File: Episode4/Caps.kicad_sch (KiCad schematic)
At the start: 190 parts

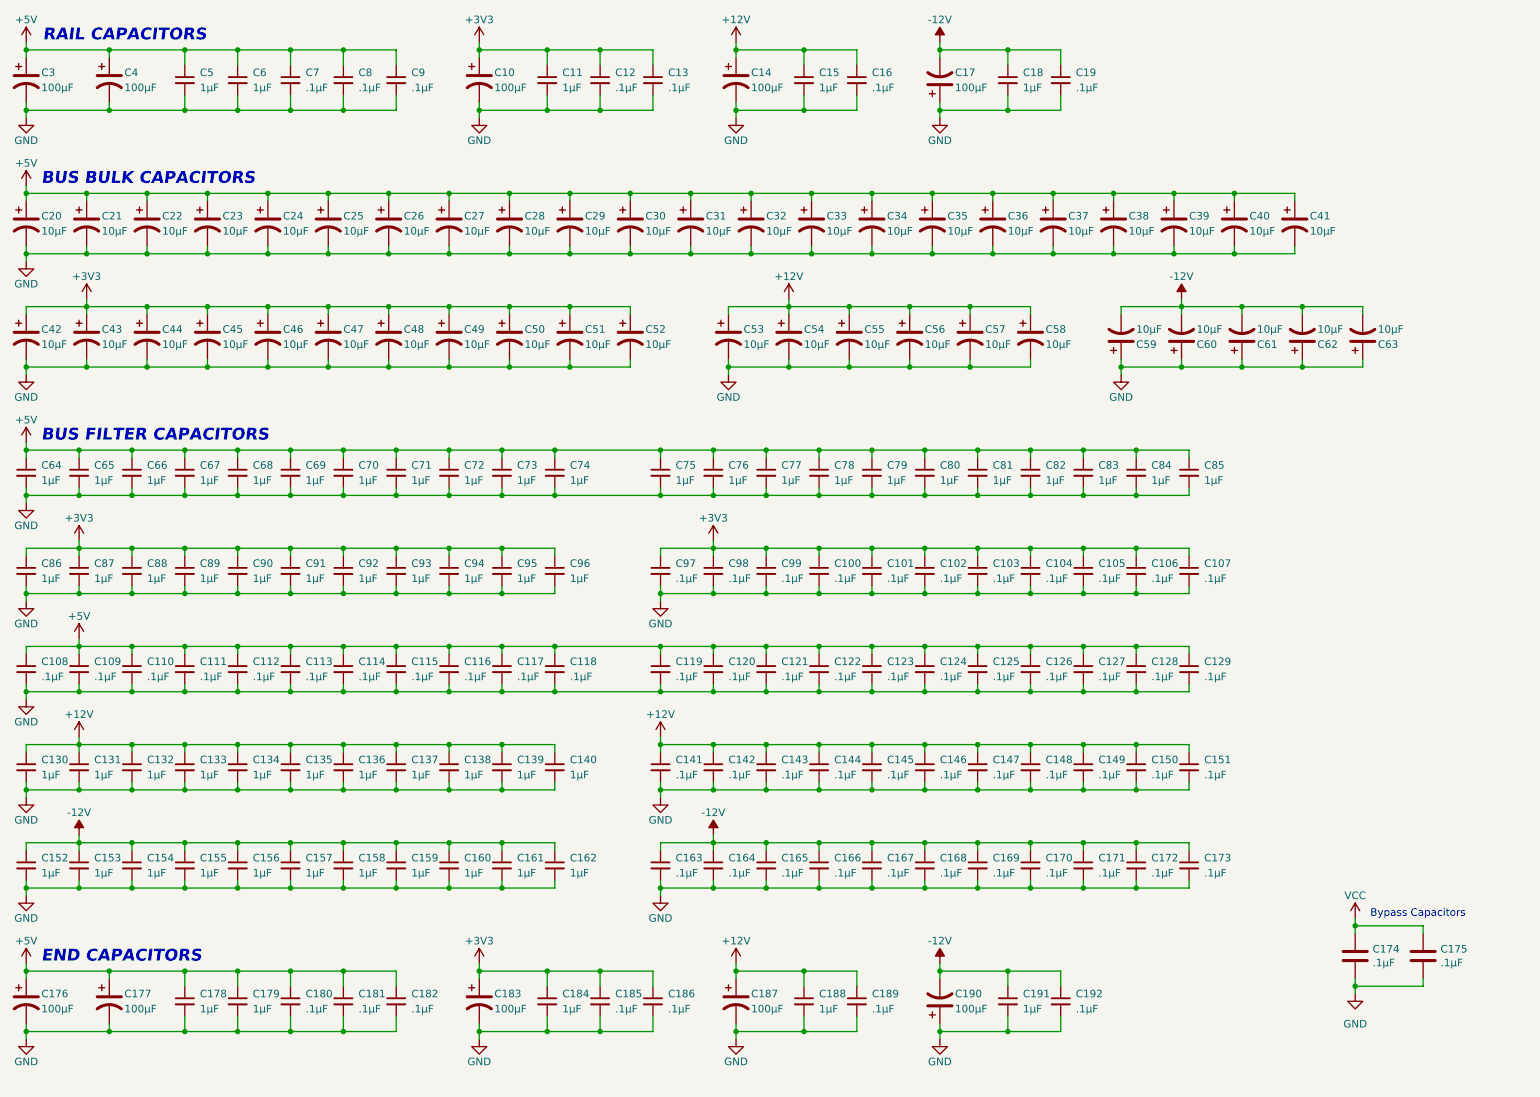
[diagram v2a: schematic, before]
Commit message: Reworked bus line order, capacitor and trace placement
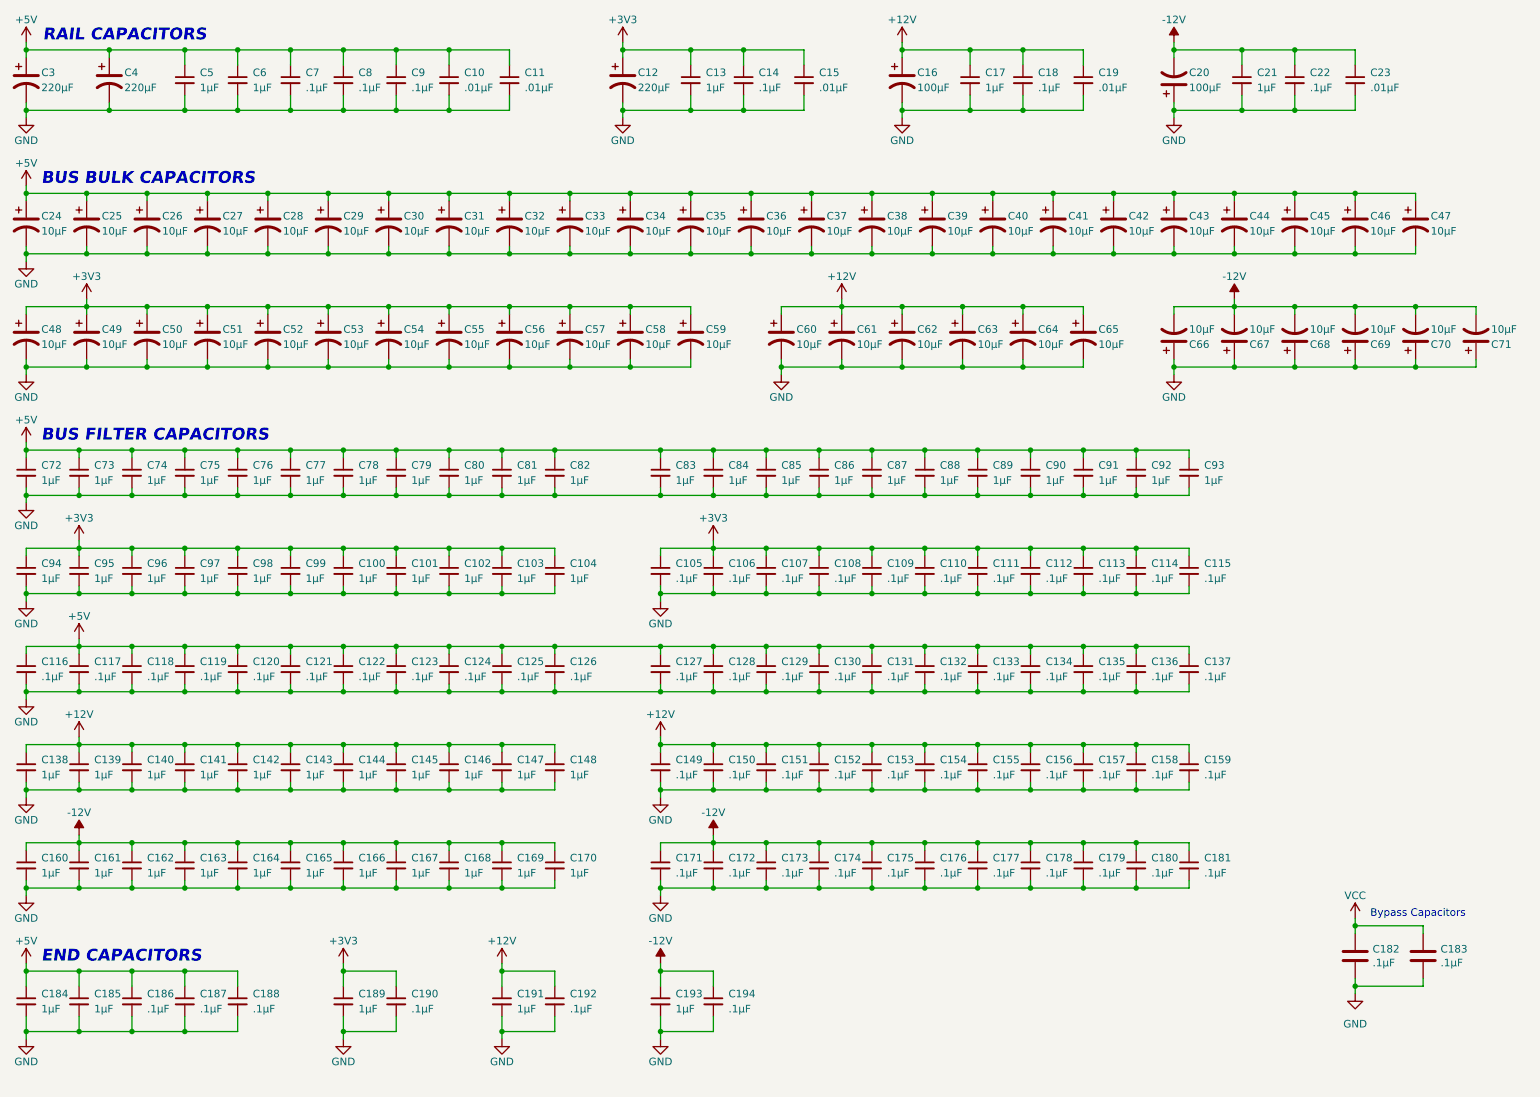
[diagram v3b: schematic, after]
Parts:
- removed C13, C186: .1µF, Capacitor_SMD:C_0805_2012Metric_Pad1.18x1.45mm_HandSolder, symbol Device:C_Small
- removed C176, C177, C183, C187, C190: 100µF, Capacitor_SMD:CP_Elec_6.3x7.7, symbol Device:C_Polarized_US
- added C10, C11, C15, C19, C23: .01µF, Capacitor_SMD:C_0805_2012Metric_Pad1.18x1.45mm_HandSolder, symbol Device:C_Small
- added C46, C47, C59, C71: 10µF, Capacitor_SMD:CP_Elec_4x5.8, symbol Device:C_Polarized_US
- C12: renamed from C10; value 100µF -> 220µF; Manufacturer_Part_Number UCD1E101MCL1GS -> UCD1C221MCL1GS
- C3, C4: value 100µF -> 220µF; Manufacturer_Part_Number UCD1E101MCL1GS -> UCD1C221MCL1GS
- renumbered C92 to C100, C93 to C101, C94 to C102, C95 to C103, C96 to C104, C97 to C105, C98 to C106, C99 to C107, C100 to C108, C101 to C109, C102 to C110, C103 to C111, C104 to C112, C105 to C113, C106 to C114, C107 to C115, C108 to C116, C109 to C117, C110 to C118, C111 to C119, C112 to C120, C113 to C121, C114 to C122, C115 to C123, C116 to C124, C117 to C125, C118 to C126, C119 to C127, C120 to C128, C121 to C129, C11 to C13, C122 to C130, C123 to C131, C124 to C132, C125 to C133, C126 to C134, C127 to C135, C128 to C136, C129 to C137, C130 to C138, C131 to C139, C12 to C14, C132 to C140, C133 to C141, C134 to C142, C135 to C143, C136 to C144, C137 to C145, C138 to C146, C139 to C147, C140 to C148, C141 to C149, C142 to C150, C143 to C151, C144 to C152, C145 to C153, C146 to C154, C147 to C155, C148 to C156, C149 to C157, C150 to C158, C151 to C159, C14 to C16, C152 to C160, C153 to C161, C154 to C162, C155 to C163, C156 to C164, C157 to C165, C158 to C166, C159 to C167, C160 to C168, C161 to C169, C15 to C17, C162 to C170, C163 to C171, C164 to C172, C165 to C173, C166 to C174, C167 to C175, C168 to C176, C169 to C177, C170 to C178, C171 to C179, C16 to C18, C172 to C180, C173 to C181, C174 to C182, C175 to C183, C178 to C184, C179 to C185, C180 to C186, C181 to C187, C182 to C188, C184 to C189, C185 to C190, C188 to C191, C189 to C192, C191 to C193, C192 to C194, C17 to C20, C18 to C21, C19 to C22, C20 to C24, C21 to C25, C22 to C26, C23 to C27, C24 to C28, C25 to C29, C26 to C30, C27 to C31, C28 to C32, C29 to C33, C30 to C34, C31 to C35, C32 to C36, C33 to C37, C34 to C38, C35 to C39, C36 to C40, C37 to C41, C38 to C42, C39 to C43, C40 to C44, C41 to C45, C42 to C48, C43 to C49, C44 to C50, C45 to C51, C46 to C52, C47 to C53, C48 to C54, C49 to C55, C50 to C56, C51 to C57, C52 to C58, C53 to C60, C54 to C61, C55 to C62, C56 to C63, C57 to C64, C58 to C65, C59 to C66, C60 to C67, C61 to C68, C62 to C69, C63 to C70, C64 to C72, C65 to C73, C66 to C74, C67 to C75, C68 to C76, C69 to C77, C70 to C78, C71 to C79, C72 to C80, C73 to C81, C74 to C82, C75 to C83, C76 to C84, C77 to C85, C78 to C86, C79 to C87, C80 to C88, C81 to C89, C82 to C90, C83 to C91, C84 to C92, C85 to C93, C86 to C94, C87 to C95, C88 to C96, C89 to C97, C90 to C98, C91 to C99
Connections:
- net +12V: now also C19.1
- net +3V3: now also C15.1, C59.1
- net +5V: now also C10.1, C11.1, C46.1, C47.1
- net -12V: now also C23.1, C71.2
- net GND: now also C10.2, C11.2, C15.2, C19.2, C23.2, C46.2, C47.2, C59.2, C71.1
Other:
- moved on the sheet: C12, C13, C14, C16, C17, C18, C184, C185, C186, C187, C188, C189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

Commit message: Finished the backplane
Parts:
- removed C144, C145, C146, C147, C148, C165, C166, C167, C168, C169, C170, C191, C193: 1µF, Capacitor_SMD:C_0805_2012Metric_Pad1.18x1.45mm_HandSolder, symbol Device:C_Small
- removed C155, C156, C159, C171, C172, C173, C174, C175, C176, C188, C192, C194, C8: .1µF, Capacitor_SMD:C_0805_2012Metric_Pad1.18x1.45mm_HandSolder, symbol Device:C_Small
- removed C182, C183: .1µF, Capacitor_SMD:C_0805_2012Metric_Pad1.18x1.45mm_HandSolder, symbol Device:C
- added C118, C129, C148, C159, C179, C28, C39, C58, C69, C8, C88, C99: 10µF, Capacitor_SMD:CP_Elec_4x5.8, symbol Device:C_Polarized_Small_US
- added C119, C128, C149, C180, C29, C38, C59, C68, C7, C89, C98: 1µF, Capacitor_SMD:C_0805_2012Metric_Pad1.18x1.45mm_HandSolder, symbol Device:C_Small
- added C120, C127, C150, C181, C30, C37, C6, C60, C67, C90, C97: 0.1µF, Capacitor_SMD:C_0805_2012Metric_Pad1.18x1.45mm_HandSolder, symbol Device:C_Small
- added C14, C15, C4, C5, C9: 10nF, Capacitor_SMD:C_0805_2012Metric_Pad1.18x1.45mm_HandSolder, symbol Device:C_Small
- C1: renamed from C46; symbol Device:C_Polarized_US -> Device:C_Polarized_Small_US
- C10: renamed from C187; value .1µF -> 0.1µF; Manufacturer_Name Samsung Electro-Mechanics -> TAIYO YUDEN; Manufacturer_Part_Number CL21B104KBFNNNG -> MCASU21GSB7104KTNA01
- C100: renamed from C110; value .1µF -> 0.1µF; Manufacturer_Name Samsung Electro-Mechanics -> TAIYO YUDEN; Manufacturer_Part_Number CL21B104KBFNNNG -> MCASU21GSB7104KTNA01
- C101: renamed from C99; Manufacturer_Name Samsung Electro-Mechanics -> TAIYO YUDEN; Manufacturer_Part_Number CL21B105KBFNNNG -> MCASU21GSB7105KTNA01
- C102: renamed from C48; symbol Device:C_Polarized_US -> Device:C_Polarized_Small_US
- C103: renamed from C67; symbol Device:C_Polarized_US -> Device:C_Polarized_Small_US
- C104: renamed from C162; Manufacturer_Name Samsung Electro-Mechanics -> TAIYO YUDEN; Manufacturer_Part_Number CL21B105KBFNNNG -> MCASU21GSB7105KTNA01
- C105: renamed from C179; value .1µF -> 0.1µF; Manufacturer_Name Samsung Electro-Mechanics -> TAIYO YUDEN; Manufacturer_Part_Number CL21B104KBFNNNG -> MCASU21GSB7104KTNA01
- C106: renamed from C132; value .1µF -> 0.1µF; Manufacturer_Name Samsung Electro-Mechanics -> TAIYO YUDEN; Manufacturer_Part_Number CL21B104KBFNNNG -> MCASU21GSB7104KTNA01
- C107: renamed from C88; Manufacturer_Name Samsung Electro-Mechanics -> TAIYO YUDEN; Manufacturer_Part_Number CL21B105KBFNNNG -> MCASU21GSB7105KTNA01
- C108: renamed from C41; symbol Device:C_Polarized_US -> Device:C_Polarized_Small_US
- C109: renamed from C26; symbol Device:C_Polarized_US -> Device:C_Polarized_Small_US
- C11: renamed from C186; value .1µF -> 0.1µF; Manufacturer_Name Samsung Electro-Mechanics -> TAIYO YUDEN; Manufacturer_Part_Number CL21B104KBFNNNG -> MCASU21GSB7104KTNA01
- C110: renamed from C80; Manufacturer_Name Samsung Electro-Mechanics -> TAIYO YUDEN; Manufacturer_Part_Number CL21B105KBFNNNG -> MCASU21GSB7105KTNA01
- C111: renamed from C126; value .1µF -> 0.1µF; Manufacturer_Name Samsung Electro-Mechanics -> TAIYO YUDEN; Manufacturer_Part_Number CL21B104KBFNNNG -> MCASU21GSB7104KTNA01
- C112: renamed from C152; value .1µF -> 0.1µF; Manufacturer_Name Samsung Electro-Mechanics -> TAIYO YUDEN; Manufacturer_Part_Number CL21B104KBFNNNG -> MCASU21GSB7104KTNA01
- C113: renamed from C141; Manufacturer_Name Samsung Electro-Mechanics -> TAIYO YUDEN; Manufacturer_Part_Number CL21B105KBFNNNG -> MCASU21GSB7105KTNA01
- C114: renamed from C62; symbol Device:C_Polarized_US -> Device:C_Polarized_Small_US
- C115: renamed from C109; value .1µF -> 0.1µF; Manufacturer_Name Samsung Electro-Mechanics -> TAIYO YUDEN; Manufacturer_Part_Number CL21B104KBFNNNG -> MCASU21GSB7104KTNA01
- C116: renamed from C98; Manufacturer_Name Samsung Electro-Mechanics -> TAIYO YUDEN; Manufacturer_Part_Number CL21B105KBFNNNG -> MCASU21GSB7105KTNA01
- C117: renamed from C58; symbol Device:C_Polarized_US -> Device:C_Polarized_Small_US
- C12: renamed from C59; symbol Device:C_Polarized_US -> Device:C_Polarized_Small_US
- C121: renamed from C131; value .1µF -> 0.1µF; Manufacturer_Name Samsung Electro-Mechanics -> TAIYO YUDEN; Manufacturer_Part_Number CL21B104KBFNNNG -> MCASU21GSB7104KTNA01
- C122: renamed from C89; Manufacturer_Name Samsung Electro-Mechanics -> TAIYO YUDEN; Manufacturer_Part_Number CL21B105KBFNNNG -> MCASU21GSB7105KTNA01
- C123: renamed from C40; symbol Device:C_Polarized_US -> Device:C_Polarized_Small_US
- C124: renamed from C35; symbol Device:C_Polarized_US -> Device:C_Polarized_Small_US
- C125: renamed from C81; Manufacturer_Name Samsung Electro-Mechanics -> TAIYO YUDEN; Manufacturer_Part_Number CL21B105KBFNNNG -> MCASU21GSB7105KTNA01
- C126: renamed from C116; value .1µF -> 0.1µF; Manufacturer_Name Samsung Electro-Mechanics -> TAIYO YUDEN; Manufacturer_Part_Number CL21B104KBFNNNG -> MCASU21GSB7104KTNA01
- C13: renamed from C71; symbol Device:C_Polarized_US -> Device:C_Polarized_Small_US
- C130: renamed from C108; value .1µF -> 0.1µF; Manufacturer_Name Samsung Electro-Mechanics -> TAIYO YUDEN; Manufacturer_Part_Number CL21B104KBFNNNG -> MCASU21GSB7104KTNA01
- C131: renamed from C97; Manufacturer_Name Samsung Electro-Mechanics -> TAIYO YUDEN; Manufacturer_Part_Number CL21B105KBFNNNG -> MCASU21GSB7105KTNA01
- C132: renamed from C49; symbol Device:C_Polarized_US -> Device:C_Polarized_Small_US
- C133: renamed from C68; symbol Device:C_Polarized_US -> Device:C_Polarized_Small_US
- C134: renamed from C161; Manufacturer_Name Samsung Electro-Mechanics -> TAIYO YUDEN; Manufacturer_Part_Number CL21B105KBFNNNG -> MCASU21GSB7105KTNA01
- C135: renamed from C178; value .1µF -> 0.1µF; Manufacturer_Name Samsung Electro-Mechanics -> TAIYO YUDEN; Manufacturer_Part_Number CL21B104KBFNNNG -> MCASU21GSB7104KTNA01
- C136: renamed from C130; value .1µF -> 0.1µF; Manufacturer_Name Samsung Electro-Mechanics -> TAIYO YUDEN; Manufacturer_Part_Number CL21B104KBFNNNG -> MCASU21GSB7104KTNA01
- C137: renamed from C90; Manufacturer_Name Samsung Electro-Mechanics -> TAIYO YUDEN; Manufacturer_Part_Number CL21B105KBFNNNG -> MCASU21GSB7105KTNA01
- C138: renamed from C39; symbol Device:C_Polarized_US -> Device:C_Polarized_Small_US
- C139: renamed from C44; symbol Device:C_Polarized_US -> Device:C_Polarized_Small_US
- C140: renamed from C82; Manufacturer_Name Samsung Electro-Mechanics -> TAIYO YUDEN; Manufacturer_Part_Number CL21B105KBFNNNG -> MCASU21GSB7105KTNA01
- C141: renamed from C117; value .1µF -> 0.1µF; Manufacturer_Name Samsung Electro-Mechanics -> TAIYO YUDEN; Manufacturer_Part_Number CL21B104KBFNNNG -> MCASU21GSB7104KTNA01
- C142: renamed from C153; value .1µF -> 0.1µF; Manufacturer_Name Samsung Electro-Mechanics -> TAIYO YUDEN; Manufacturer_Part_Number CL21B104KBFNNNG -> MCASU21GSB7104KTNA01
- C143: renamed from C142; Manufacturer_Name Samsung Electro-Mechanics -> TAIYO YUDEN; Manufacturer_Part_Number CL21B105KBFNNNG -> MCASU21GSB7105KTNA01
- C144: renamed from C64; symbol Device:C_Polarized_US -> Device:C_Polarized_Small_US
- C145: renamed from C107; value .1µF -> 0.1µF; Manufacturer_Name Samsung Electro-Mechanics -> TAIYO YUDEN; Manufacturer_Part_Number CL21B104KBFNNNG -> MCASU21GSB7104KTNA01
- C146: renamed from C96; Manufacturer_Name Samsung Electro-Mechanics -> TAIYO YUDEN; Manufacturer_Part_Number CL21B105KBFNNNG -> MCASU21GSB7105KTNA01
- C147: renamed from C50; symbol Device:C_Polarized_US -> Device:C_Polarized_Small_US
- C151: renamed from C129; value .1µF -> 0.1µF; Manufacturer_Name Samsung Electro-Mechanics -> TAIYO YUDEN; Manufacturer_Part_Number CL21B104KBFNNNG -> MCASU21GSB7104KTNA01
- C152: renamed from C91; Manufacturer_Name Samsung Electro-Mechanics -> TAIYO YUDEN; Manufacturer_Part_Number CL21B105KBFNNNG -> MCASU21GSB7105KTNA01
- C153: renamed from C38; symbol Device:C_Polarized_US -> Device:C_Polarized_Small_US
- C154: renamed from C27; symbol Device:C_Polarized_US -> Device:C_Polarized_Small_US
- C155: renamed from C72; Manufacturer_Name Samsung Electro-Mechanics -> TAIYO YUDEN; Manufacturer_Part_Number CL21B105KBFNNNG -> MCASU21GSB7105KTNA01
- C156: renamed from C118; value .1µF -> 0.1µF; Manufacturer_Name Samsung Electro-Mechanics -> TAIYO YUDEN; Manufacturer_Part_Number CL21B104KBFNNNG -> MCASU21GSB7104KTNA01
- C157: value .1µF -> 0.1µF; Manufacturer_Name Samsung Electro-Mechanics -> TAIYO YUDEN; Manufacturer_Part_Number CL21B104KBFNNNG -> MCASU21GSB7104KTNA01
- C158: value .1µF -> 1µF; Manufacturer_Name Samsung Electro-Mechanics -> TAIYO YUDEN; Manufacturer_Part_Number CL21B104KBFNNNG -> MCASU21GSB7105KTNA01
- C16: renamed from C189; Manufacturer_Name Samsung Electro-Mechanics -> TAIYO YUDEN; Manufacturer_Part_Number CL21B105KBFNNNG -> MCASU21GSB7105KTNA01
- C160: renamed from C106; value .1µF -> 0.1µF; Manufacturer_Name Samsung Electro-Mechanics -> TAIYO YUDEN; Manufacturer_Part_Number CL21B104KBFNNNG -> MCASU21GSB7104KTNA01
- C161: renamed from C95; Manufacturer_Name Samsung Electro-Mechanics -> TAIYO YUDEN; Manufacturer_Part_Number CL21B105KBFNNNG -> MCASU21GSB7105KTNA01
- C162: renamed from C51; symbol Device:C_Polarized_US -> Device:C_Polarized_Small_US
- C163: renamed from C69; symbol Device:C_Polarized_US -> Device:C_Polarized_Small_US
- C164: renamed from C160; Manufacturer_Name Samsung Electro-Mechanics -> TAIYO YUDEN; Manufacturer_Part_Number CL21B105KBFNNNG -> MCASU21GSB7105KTNA01
- C165: renamed from C177; value .1µF -> 0.1µF; Manufacturer_Name Samsung Electro-Mechanics -> TAIYO YUDEN; Manufacturer_Part_Number CL21B104KBFNNNG -> MCASU21GSB7104KTNA01
- C166: renamed from C128; value .1µF -> 0.1µF; Manufacturer_Name Samsung Electro-Mechanics -> TAIYO YUDEN; Manufacturer_Part_Number CL21B104KBFNNNG -> MCASU21GSB7104KTNA01
- C167: renamed from C92; Manufacturer_Name Samsung Electro-Mechanics -> TAIYO YUDEN; Manufacturer_Part_Number CL21B105KBFNNNG -> MCASU21GSB7105KTNA01
- C168: renamed from C37; symbol Device:C_Polarized_US -> Device:C_Polarized_Small_US
- C17: renamed from C185; Manufacturer_Name Samsung Electro-Mechanics -> TAIYO YUDEN; Manufacturer_Part_Number CL21B105KBFNNNG -> MCASU21GSB7105KTNA01
- C170: renamed from C36; symbol Device:C_Polarized_US -> Device:C_Polarized_Small_US
- C171: renamed from C73; Manufacturer_Name Samsung Electro-Mechanics -> TAIYO YUDEN; Manufacturer_Part_Number CL21B105KBFNNNG -> MCASU21GSB7105KTNA01
- C172: renamed from C119; value .1µF -> 0.1µF; Manufacturer_Name Samsung Electro-Mechanics -> TAIYO YUDEN; Manufacturer_Part_Number CL21B104KBFNNNG -> MCASU21GSB7104KTNA01
- C173: renamed from C154; value .1µF -> 0.1µF; Manufacturer_Name Samsung Electro-Mechanics -> TAIYO YUDEN; Manufacturer_Part_Number CL21B104KBFNNNG -> MCASU21GSB7104KTNA01
- C174: renamed from C143; Manufacturer_Name Samsung Electro-Mechanics -> TAIYO YUDEN; Manufacturer_Part_Number CL21B105KBFNNNG -> MCASU21GSB7105KTNA01
- C175: renamed from C65; symbol Device:C_Polarized_US -> Device:C_Polarized_Small_US
- C176: renamed from C105; value .1µF -> 0.1µF; Manufacturer_Name Samsung Electro-Mechanics -> TAIYO YUDEN; Manufacturer_Part_Number CL21B104KBFNNNG -> MCASU21GSB7104KTNA01
- C177: renamed from C94; Manufacturer_Name Samsung Electro-Mechanics -> TAIYO YUDEN; Manufacturer_Part_Number CL21B105KBFNNNG -> MCASU21GSB7105KTNA01
- C178: renamed from C52; symbol Device:C_Polarized_US -> Device:C_Polarized_Small_US
- C18: renamed from C47; symbol Device:C_Polarized_US -> Device:C_Polarized_Small_US
- C182: renamed from C127; value .1µF -> 0.1µF; Manufacturer_Name Samsung Electro-Mechanics -> TAIYO YUDEN; Manufacturer_Part_Number CL21B104KBFNNNG -> MCASU21GSB7104KTNA01
- C183: renamed from C93; Manufacturer_Name Samsung Electro-Mechanics -> TAIYO YUDEN; Manufacturer_Part_Number CL21B105KBFNNNG -> MCASU21GSB7105KTNA01
- C184: renamed from C45; symbol Device:C_Polarized_US -> Device:C_Polarized_Small_US
- C187: renamed from C3; symbol Device:C_Polarized_US -> Device:C_Polarized_Small_US
- C188: renamed from C12; symbol Device:C_Polarized_US -> Device:C_Polarized_Small_US
- C189: renamed from C16; symbol Device:C_Polarized_US -> Device:C_Polarized_Small_US
- C19: renamed from C24; symbol Device:C_Polarized_US -> Device:C_Polarized_Small_US
- C190: renamed from C4; symbol Device:C_Polarized_US -> Device:C_Polarized_Small_US
- C192: renamed from C5; Manufacturer_Name Samsung Electro-Mechanics -> TAIYO YUDEN; Manufacturer_Part_Number CL21B105KBFNNNG -> MCASU21GSB7105KTNA01
- C193: renamed from C13; Manufacturer_Name Samsung Electro-Mechanics -> TAIYO YUDEN; Manufacturer_Part_Number CL21B105KBFNNNG -> MCASU21GSB7105KTNA01
- C194: renamed from C17; Manufacturer_Name Samsung Electro-Mechanics -> TAIYO YUDEN; Manufacturer_Part_Number CL21B105KBFNNNG -> MCASU21GSB7105KTNA01
- C195: renamed from C7; value .1µF -> 0.1µF; Manufacturer_Name Samsung Electro-Mechanics -> TAIYO YUDEN; Manufacturer_Part_Number CL21B104KBFNNNG -> MCASU21GSB7104KTNA01
- C196: renamed from C14; value .1µF -> 0.1µF; Manufacturer_Name Samsung Electro-Mechanics -> TAIYO YUDEN; Manufacturer_Part_Number CL21B104KBFNNNG -> MCASU21GSB7104KTNA01
- C197: renamed from C18; value .1µF -> 0.1µF; Manufacturer_Name Samsung Electro-Mechanics -> TAIYO YUDEN; Manufacturer_Part_Number CL21B104KBFNNNG -> MCASU21GSB7104KTNA01
- C198: renamed from C10; value .01µF -> 10nF; Manufacturer_Name Samsung Electro-Mechanics -> TAIYO YUDEN; Manufacturer_Part_Number CL21B103KBCNNNC -> MCASU21GSB7103KTNA01
- C199: renamed from C15; value .01µF -> 10nF; Manufacturer_Name Samsung Electro-Mechanics -> TAIYO YUDEN; Manufacturer_Part_Number CL21B103KBCNNNC -> MCASU21GSB7103KTNA01
- C2: renamed from C184; Manufacturer_Name Samsung Electro-Mechanics -> TAIYO YUDEN; Manufacturer_Part_Number CL21B105KBFNNNG -> MCASU21GSB7105KTNA01
- C20: renamed from C74; Manufacturer_Name Samsung Electro-Mechanics -> TAIYO YUDEN; Manufacturer_Part_Number CL21B105KBFNNNG -> MCASU21GSB7105KTNA01
- C200: renamed from C19; value .01µF -> 10nF; Manufacturer_Name Samsung Electro-Mechanics -> TAIYO YUDEN; Manufacturer_Part_Number CL21B103KBCNNNC -> MCASU21GSB7103KTNA01
- C201: renamed from C20; symbol Device:C_Polarized_US -> Device:C_Polarized_Small_US
- C202: renamed from C6; Manufacturer_Name Samsung Electro-Mechanics -> TAIYO YUDEN; Manufacturer_Part_Number CL21B105KBFNNNG -> MCASU21GSB7105KTNA01
- C203: renamed from C9; value .1µF -> 0.1µF; Manufacturer_Name Samsung Electro-Mechanics -> TAIYO YUDEN; Manufacturer_Part_Number CL21B104KBFNNNG -> MCASU21GSB7104KTNA01
- C204: renamed from C11; value .01µF -> 10nF; Manufacturer_Name Samsung Electro-Mechanics -> TAIYO YUDEN; Manufacturer_Part_Number CL21B103KBCNNNC -> MCASU21GSB7103KTNA01
- C205: renamed from C21; Manufacturer_Name Samsung Electro-Mechanics -> TAIYO YUDEN; Manufacturer_Part_Number CL21B105KBFNNNG -> MCASU21GSB7105KTNA01
- C206: renamed from C22; value .1µF -> 0.1µF; Manufacturer_Name Samsung Electro-Mechanics -> TAIYO YUDEN; Manufacturer_Part_Number CL21B104KBFNNNG -> MCASU21GSB7104KTNA01
- C207: renamed from C23; value .01µF -> 10nF; Manufacturer_Name Samsung Electro-Mechanics -> TAIYO YUDEN; Manufacturer_Part_Number CL21B103KBCNNNC -> MCASU21GSB7103KTNA01
- C21: renamed from C120; value .1µF -> 0.1µF; Manufacturer_Name Samsung Electro-Mechanics -> TAIYO YUDEN; Manufacturer_Part_Number CL21B104KBFNNNG -> MCASU21GSB7104KTNA01
- C22: renamed from C149; value .1µF -> 0.1µF; Manufacturer_Name Samsung Electro-Mechanics -> TAIYO YUDEN; Manufacturer_Part_Number CL21B104KBFNNNG -> MCASU21GSB7104KTNA01
- C23: renamed from C138; Manufacturer_Name Samsung Electro-Mechanics -> TAIYO YUDEN; Manufacturer_Part_Number CL21B105KBFNNNG -> MCASU21GSB7105KTNA01
- C24: renamed from C63; symbol Device:C_Polarized_US -> Device:C_Polarized_Small_US
- C25: renamed from C115; value .1µF -> 0.1µF; Manufacturer_Name Samsung Electro-Mechanics -> TAIYO YUDEN; Manufacturer_Part_Number CL21B104KBFNNNG -> MCASU21GSB7104KTNA01
- C26: renamed from C104; Manufacturer_Name Samsung Electro-Mechanics -> TAIYO YUDEN; Manufacturer_Part_Number CL21B105KBFNNNG -> MCASU21GSB7105KTNA01
- C27: renamed from C53; symbol Device:C_Polarized_US -> Device:C_Polarized_Small_US
- C3: renamed from C190; value .1µF -> 0.1µF; Manufacturer_Name Samsung Electro-Mechanics -> TAIYO YUDEN; Manufacturer_Part_Number CL21B104KBFNNNG -> MCASU21GSB7104KTNA01
- C31: renamed from C137; value .1µF -> 0.1µF; Manufacturer_Name Samsung Electro-Mechanics -> TAIYO YUDEN; Manufacturer_Part_Number CL21B104KBFNNNG -> MCASU21GSB7104KTNA01
- C32: renamed from C83; Manufacturer_Name Samsung Electro-Mechanics -> TAIYO YUDEN; Manufacturer_Part_Number CL21B105KBFNNNG -> MCASU21GSB7105KTNA01
- C33: renamed from C32; symbol Device:C_Polarized_US -> Device:C_Polarized_Small_US
- C34: renamed from C33; symbol Device:C_Polarized_US -> Device:C_Polarized_Small_US
- C35: renamed from C75; Manufacturer_Name Samsung Electro-Mechanics -> TAIYO YUDEN; Manufacturer_Part_Number CL21B105KBFNNNG -> MCASU21GSB7105KTNA01
- C36: renamed from C121; value .1µF -> 0.1µF; Manufacturer_Name Samsung Electro-Mechanics -> TAIYO YUDEN; Manufacturer_Part_Number CL21B104KBFNNNG -> MCASU21GSB7104KTNA01
- C40: renamed from C114; value .1µF -> 0.1µF; Manufacturer_Name Samsung Electro-Mechanics -> TAIYO YUDEN; Manufacturer_Part_Number CL21B104KBFNNNG -> MCASU21GSB7104KTNA01
- C41: renamed from C103; Manufacturer_Name Samsung Electro-Mechanics -> TAIYO YUDEN; Manufacturer_Part_Number CL21B105KBFNNNG -> MCASU21GSB7105KTNA01
- C42: renamed from C54; symbol Device:C_Polarized_US -> Device:C_Polarized_Small_US
- C43: renamed from C70; symbol Device:C_Polarized_US -> Device:C_Polarized_Small_US
- C44: renamed from C164; Manufacturer_Name Samsung Electro-Mechanics -> TAIYO YUDEN; Manufacturer_Part_Number CL21B105KBFNNNG -> MCASU21GSB7105KTNA01
- C45: renamed from C181; value .1µF -> 0.1µF; Manufacturer_Name Samsung Electro-Mechanics -> TAIYO YUDEN; Manufacturer_Part_Number CL21B104KBFNNNG -> MCASU21GSB7104KTNA01
- C46: renamed from C136; value .1µF -> 0.1µF; Manufacturer_Name Samsung Electro-Mechanics -> TAIYO YUDEN; Manufacturer_Part_Number CL21B104KBFNNNG -> MCASU21GSB7104KTNA01
- C47: renamed from C84; Manufacturer_Name Samsung Electro-Mechanics -> TAIYO YUDEN; Manufacturer_Part_Number CL21B105KBFNNNG -> MCASU21GSB7105KTNA01
- C48: renamed from C31; symbol Device:C_Polarized_US -> Device:C_Polarized_Small_US
- C49: renamed from C42; symbol Device:C_Polarized_US -> Device:C_Polarized_Small_US
- C50: renamed from C76; Manufacturer_Name Samsung Electro-Mechanics -> TAIYO YUDEN; Manufacturer_Part_Number CL21B105KBFNNNG -> MCASU21GSB7105KTNA01
- C51: renamed from C122; value .1µF -> 0.1µF; Manufacturer_Name Samsung Electro-Mechanics -> TAIYO YUDEN; Manufacturer_Part_Number CL21B104KBFNNNG -> MCASU21GSB7104KTNA01
- C52: renamed from C151; value .1µF -> 0.1µF; Manufacturer_Name Samsung Electro-Mechanics -> TAIYO YUDEN; Manufacturer_Part_Number CL21B104KBFNNNG -> MCASU21GSB7104KTNA01
- C53: renamed from C140; Manufacturer_Name Samsung Electro-Mechanics -> TAIYO YUDEN; Manufacturer_Part_Number CL21B105KBFNNNG -> MCASU21GSB7105KTNA01
- C54: renamed from C60; symbol Device:C_Polarized_US -> Device:C_Polarized_Small_US
- C55: renamed from C113; value .1µF -> 0.1µF; Manufacturer_Name Samsung Electro-Mechanics -> TAIYO YUDEN; Manufacturer_Part_Number CL21B104KBFNNNG -> MCASU21GSB7104KTNA01
- C56: renamed from C102; Manufacturer_Name Samsung Electro-Mechanics -> TAIYO YUDEN; Manufacturer_Part_Number CL21B105KBFNNNG -> MCASU21GSB7105KTNA01
- C57: renamed from C55; symbol Device:C_Polarized_US -> Device:C_Polarized_Small_US
- C61: renamed from C135; value .1µF -> 0.1µF; Manufacturer_Name Samsung Electro-Mechanics -> TAIYO YUDEN; Manufacturer_Part_Number CL21B104KBFNNNG -> MCASU21GSB7104KTNA01
- C62: renamed from C85; Manufacturer_Name Samsung Electro-Mechanics -> TAIYO YUDEN; Manufacturer_Part_Number CL21B105KBFNNNG -> MCASU21GSB7105KTNA01
- C63: renamed from C30; symbol Device:C_Polarized_US -> Device:C_Polarized_Small_US
- C64: renamed from C25; symbol Device:C_Polarized_US -> Device:C_Polarized_Small_US
- C65: renamed from C77; Manufacturer_Name Samsung Electro-Mechanics -> TAIYO YUDEN; Manufacturer_Part_Number CL21B105KBFNNNG -> MCASU21GSB7105KTNA01
- C66: renamed from C123; value .1µF -> 0.1µF; Manufacturer_Name Samsung Electro-Mechanics -> TAIYO YUDEN; Manufacturer_Part_Number CL21B104KBFNNNG -> MCASU21GSB7104KTNA01
- C70: renamed from C112; value .1µF -> 0.1µF; Manufacturer_Name Samsung Electro-Mechanics -> TAIYO YUDEN; Manufacturer_Part_Number CL21B104KBFNNNG -> MCASU21GSB7104KTNA01
- C71: renamed from C101; Manufacturer_Name Samsung Electro-Mechanics -> TAIYO YUDEN; Manufacturer_Part_Number CL21B105KBFNNNG -> MCASU21GSB7105KTNA01
- C72: renamed from C56; symbol Device:C_Polarized_US -> Device:C_Polarized_Small_US
- C73: renamed from C66; symbol Device:C_Polarized_US -> Device:C_Polarized_Small_US
- C74: renamed from C163; Manufacturer_Name Samsung Electro-Mechanics -> TAIYO YUDEN; Manufacturer_Part_Number CL21B105KBFNNNG -> MCASU21GSB7105KTNA01
- C75: renamed from C180; value .1µF -> 0.1µF; Manufacturer_Name Samsung Electro-Mechanics -> TAIYO YUDEN; Manufacturer_Part_Number CL21B104KBFNNNG -> MCASU21GSB7104KTNA01
- C76: renamed from C134; value .1µF -> 0.1µF; Manufacturer_Name Samsung Electro-Mechanics -> TAIYO YUDEN; Manufacturer_Part_Number CL21B104KBFNNNG -> MCASU21GSB7104KTNA01
- C77: renamed from C86; Manufacturer_Name Samsung Electro-Mechanics -> TAIYO YUDEN; Manufacturer_Part_Number CL21B105KBFNNNG -> MCASU21GSB7105KTNA01
- C78: renamed from C29; symbol Device:C_Polarized_US -> Device:C_Polarized_Small_US
- C79: renamed from C34; symbol Device:C_Polarized_US -> Device:C_Polarized_Small_US
- C80: renamed from C78; Manufacturer_Name Samsung Electro-Mechanics -> TAIYO YUDEN; Manufacturer_Part_Number CL21B105KBFNNNG -> MCASU21GSB7105KTNA01
- C81: renamed from C124; value .1µF -> 0.1µF; Manufacturer_Name Samsung Electro-Mechanics -> TAIYO YUDEN; Manufacturer_Part_Number CL21B104KBFNNNG -> MCASU21GSB7104KTNA01
- C82: renamed from C150; value .1µF -> 0.1µF; Manufacturer_Name Samsung Electro-Mechanics -> TAIYO YUDEN; Manufacturer_Part_Number CL21B104KBFNNNG -> MCASU21GSB7104KTNA01
- C83: renamed from C139; Manufacturer_Name Samsung Electro-Mechanics -> TAIYO YUDEN; Manufacturer_Part_Number CL21B105KBFNNNG -> MCASU21GSB7105KTNA01
- C84: renamed from C61; symbol Device:C_Polarized_US -> Device:C_Polarized_Small_US
- C85: renamed from C111; value .1µF -> 0.1µF; Manufacturer_Name Samsung Electro-Mechanics -> TAIYO YUDEN; Manufacturer_Part_Number CL21B104KBFNNNG -> MCASU21GSB7104KTNA01
- C86: renamed from C100; Manufacturer_Name Samsung Electro-Mechanics -> TAIYO YUDEN; Manufacturer_Part_Number CL21B105KBFNNNG -> MCASU21GSB7105KTNA01
- C87: renamed from C57; symbol Device:C_Polarized_US -> Device:C_Polarized_Small_US
- C91: renamed from C133; value .1µF -> 0.1µF; Manufacturer_Name Samsung Electro-Mechanics -> TAIYO YUDEN; Manufacturer_Part_Number CL21B104KBFNNNG -> MCASU21GSB7104KTNA01
- C92: renamed from C87; Manufacturer_Name Samsung Electro-Mechanics -> TAIYO YUDEN; Manufacturer_Part_Number CL21B105KBFNNNG -> MCASU21GSB7105KTNA01
- C93: renamed from C28; symbol Device:C_Polarized_US -> Device:C_Polarized_Small_US
- C94: renamed from C43; symbol Device:C_Polarized_US -> Device:C_Polarized_Small_US
- C95: renamed from C79; Manufacturer_Name Samsung Electro-Mechanics -> TAIYO YUDEN; Manufacturer_Part_Number CL21B105KBFNNNG -> MCASU21GSB7105KTNA01
- C96: renamed from C125; value .1µF -> 0.1µF; Manufacturer_Name Samsung Electro-Mechanics -> TAIYO YUDEN; Manufacturer_Part_Number CL21B104KBFNNNG -> MCASU21GSB7104KTNA01
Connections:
- net +12V: now also C127.1, C128.1, C129.1, C159.1, C37.1, C38.1, C39.1, C5.1, C6.1, C67.1, C68.1, C69.1, C7.1, C8.1, C97.1, C98.1, C99.1
- net +3V3: now also C10.1, C11.1, C9.1; no longer C16.1, C3.1
- net +5V: now also C16.1, C3.1, C15.1, C4.1; no longer C10.1, C11.1
- net -12V: now also C118.2, C119.1, C120.1, C14.1, C148.2, C149.1, C150.1, C179.2, C180.1, C181.1, C28.2, C29.1, C30.1, C58.2, C59.1, C60.1, C88.2, C89.1, C90.1
- net GND: now also C118.1, C119.2, C120.2, C127.2, C128.2, C129.2, C14.2, C148.1, C149.2, C15.2, C150.2, C159.2, C179.1, C180.2, C181.2, C28.1, C29.2, C30.2, C37.2, C38.2, C39.2, C4.2, C5.2, C58.1, C59.2, C6.2, C60.2, C67.2, C68.2, C69.2, C7.2, C8.2, C88.1, C89.2, C9.2, C90.2, C97.2, C98.2, C99.2
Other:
- note added: "PSU CAPACITORS"
- note removed: "Bypass Capacitors"
- note removed: "END CAPACITORS"
- note removed: "RAIL CAPACITORS"
- moved on the sheet: C1, C10, C100, C101, C102, C103, C104, C105, C106, C107, C108, C109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

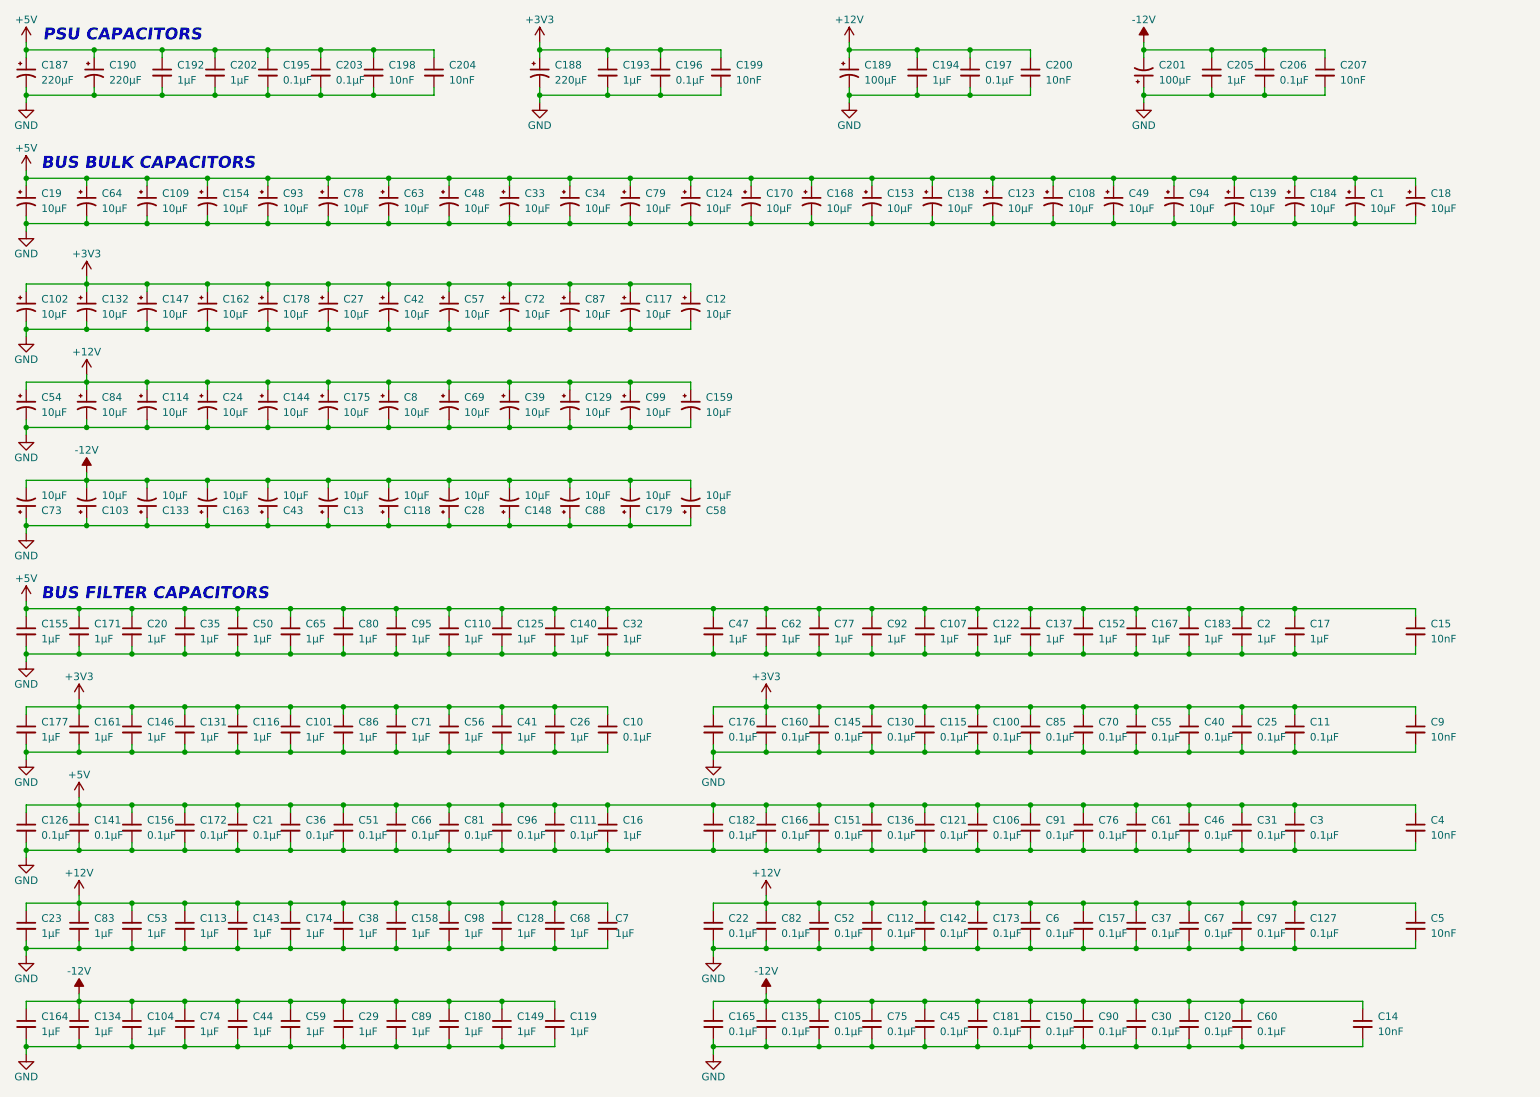
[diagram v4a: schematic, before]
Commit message: Moved power traces from inner CU to back CU
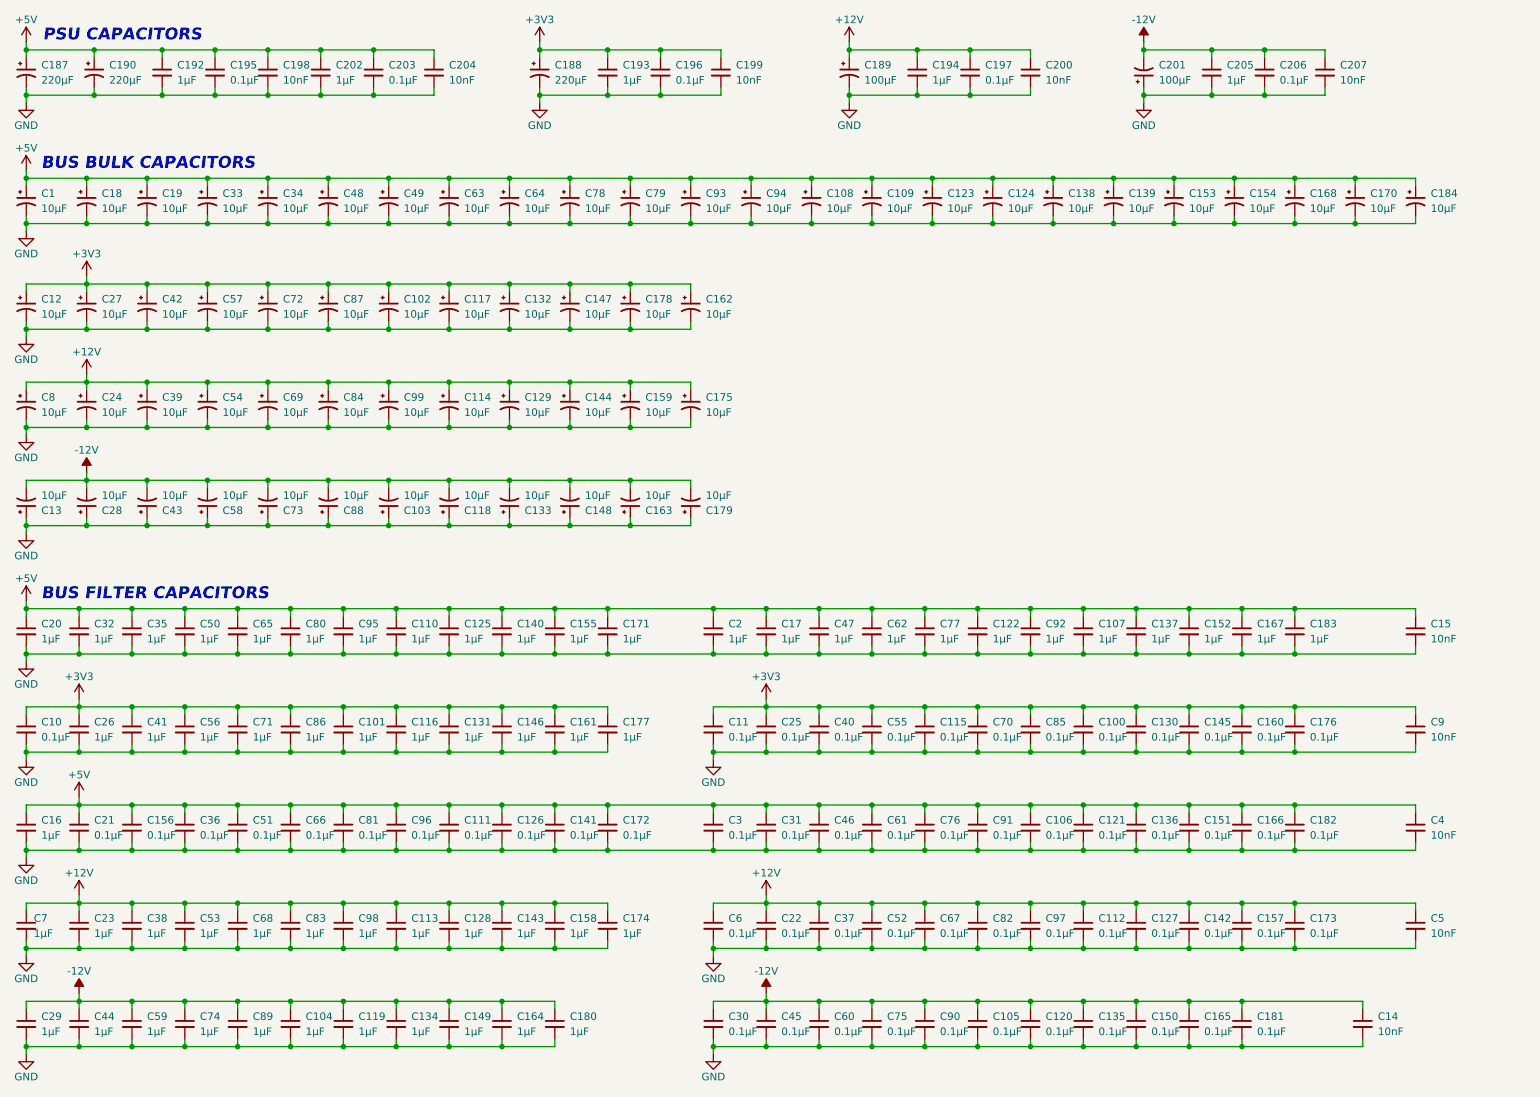
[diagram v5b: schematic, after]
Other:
- moved on the sheet: C1, C10, C100, C101, C102, C103, C104, C105, C106, C107, C108, C109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
